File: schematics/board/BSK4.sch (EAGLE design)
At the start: 32 parts

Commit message: Платы подготовлены для Резонита
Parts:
- renumbered U$10 to FS8205A#2, U$5 to DS18B20Z, U$8 to L293DD, U$9 to FS8205A#1
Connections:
- removed net HEAT: DS18B20Z.HEAT, FS8205A#1.HEAT, FS8205A#2.HEAT, L293DD.HEAT
- net GND: now also DS18B20Z.HEAT, FS8205A#1.HEAT, FS8205A#2.HEAT, L293DD.HEAT

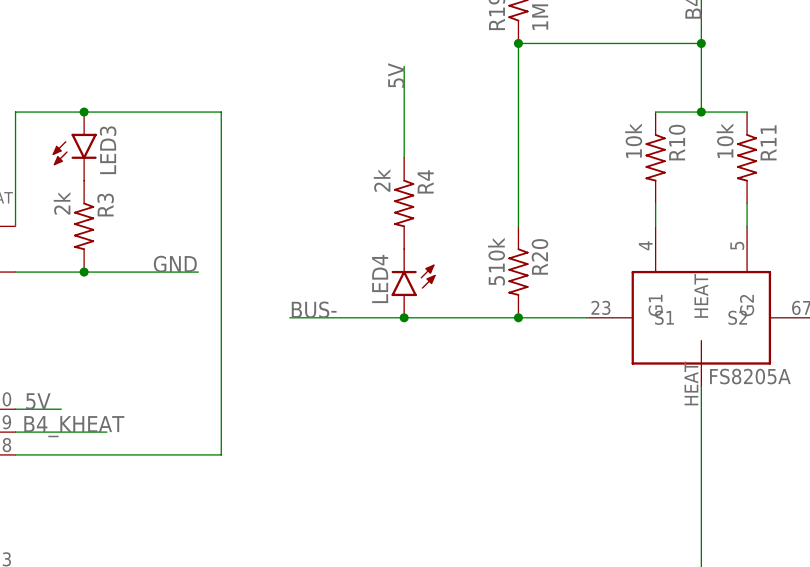
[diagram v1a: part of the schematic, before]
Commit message: Исправлены RADIO и диоды
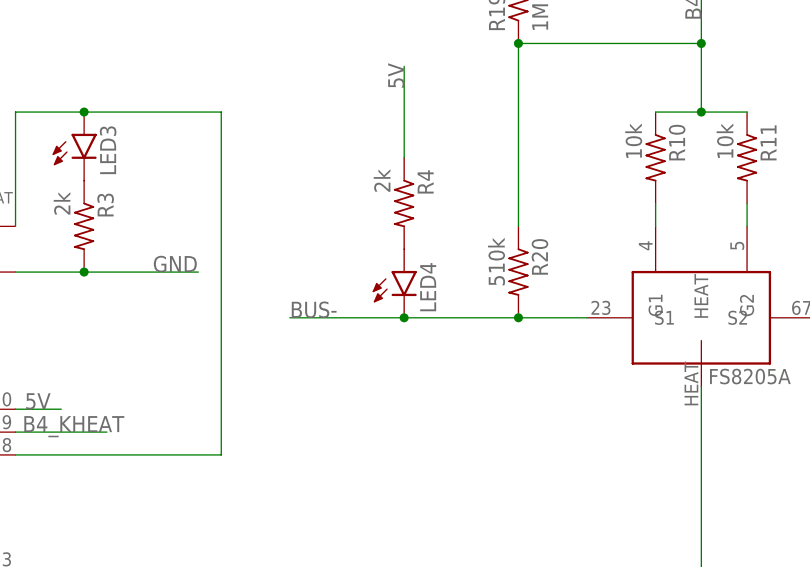
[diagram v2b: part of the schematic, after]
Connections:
- net BUS-: now also LED4.C; no longer LED4.A
- net N$27: now also LED4.A; no longer LED4.C
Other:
- moved on the sheet: LED4
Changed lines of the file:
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@@
 <part name="R3" library="resistor" library_urn="urn:adsk.eagle:library:348" deviceset="R-US_" device="R0603" package3d_urn="urn:adsk.eagle:package:23555/3" value="2k"/>
 <part name="LED3" library="led" library_urn="urn:adsk.eagle:library:259" deviceset="LED" device="CHIPLED_0603" package3d_urn="urn:adsk.eagle:package:15822/2"/>
-<part name="LED4" library="led" library_urn="urn:adsk.eagle:library:259" deviceset="LED" device="CHIPLED_0603" package3d_urn="urn:adsk.eagle:package:15822/2"/>
 <part name="R4" library="resistor" library_urn="urn:adsk.eagle:library:348" deviceset="R-US_" device="R0603" package3d_urn="urn:adsk.eagle:package:23555/3" value="2k"/>
 <part name="LED5" library="led" library_urn="urn:adsk.eagle:library:259" deviceset="LED" device="CHIPLED_0603" package3d_urn="urn:adsk.eagle:package:15822/2"/>
 <part name="R5" library="resistor" library_urn="urn:adsk.eagle:library:348" deviceset="R-US_" device="R0603" package3d_urn="urn:adsk.eagle:package:23555/3" value="2k"/>
+<part name="LED4" library="led" library_urn="urn:adsk.eagle:library:259" deviceset="LED" device="CHIPLED_0603" package3d_urn="urn:adsk.eagle:package:15822/2"/>
 </parts>
 <sheets>
@@
 <attribute name="VALUE" x="92.075" y="234.188" size="1.778" layer="96" rot="R90"/>
 </instance>
-<instance part="LED4" gate="G$1" x="121.92" y="220.98" smashed="yes" rot="R180">
-<attribute name="NAME" x="118.364" y="225.552" size="1.778" layer="95" rot="R270"/>
-<attribute name="VALUE" x="116.205" y="225.552" size="1.778" layer="96" rot="R270"/>
-</instance>
 <instance part="R4" gate="G$1" x="121.92" y="231.14" smashed="yes" rot="R270">
 <attribute name="NAME" x="123.4186" y="234.95" size="1.778" layer="95" rot="R270"/>
@@
 <attribute name="NAME" x="161.5186" y="173.99" size="1.778" layer="95" rot="R270"/>
 <attribute name="VALUE" x="156.718" y="173.99" size="1.778" layer="96" rot="R270"/>
+</instance>
+<instance part="LED4" gate="G$1" x="121.92" y="223.52" smashed="yes">
+<attribute name="NAME" x="125.476" y="218.948" size="1.778" layer="95" rot="R90"/>
+<attribute name="VALUE" x="127.635" y="218.948" size="1.778" layer="96" rot="R90"/>
 </instance>
 </instances>
@@
 <wire x1="134.62" y1="218.44" x2="142.24" y2="218.44" width="0.1524" layer="91"/>
 <pinref part="R20" gate="G$1" pin="2"/>
-<wire x1="134.62" y1="218.44" x2="121.92" y2="218.44" width="0.1524" layer="91"/>
 <junction x="134.62" y="218.44"/>
 <label x="109.22" y="218.44" size="1.778" layer="95"/>
 <pinref part="FS8205A#1" gate="G$1" pin="S1"/>
-<pinref part="LED4" gate="G$1" pin="A"/>
+<wire x1="134.62" y1="218.44" x2="121.92" y2="218.44" width="0.1524" layer="91"/>
+<pinref part="LED4" gate="G$1" pin="C"/>
 <wire x1="121.92" y1="218.44" x2="109.22" y2="218.44" width="0.1524" layer="91"/>
 <junction x="121.92" y="218.44"/>
@@
 </segment>
 </net>
-<net name="N$27" class="0">
-<segment>
-<pinref part="R4" gate="G$1" pin="2"/>
-<pinref part="LED4" gate="G$1" pin="C"/>
-</segment>
-</net>
 <net name="N$28" class="0">
 <segment>
@@
 </segment>
 </net>
+<net name="N$27" class="0">
+<segment>
+<pinref part="LED4" gate="G$1" pin="A"/>
+<pinref part="R4" gate="G$1" pin="2"/>
+</segment>
+</net>

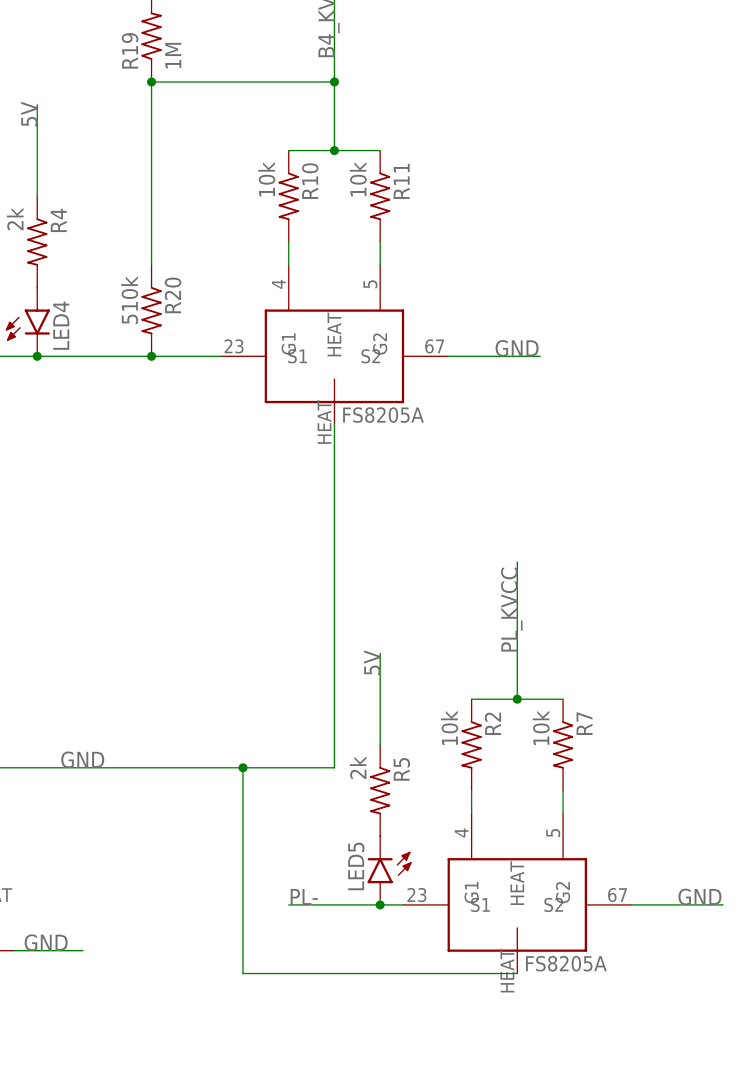
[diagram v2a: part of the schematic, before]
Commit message: Резисторы у FS8205A 100Ом
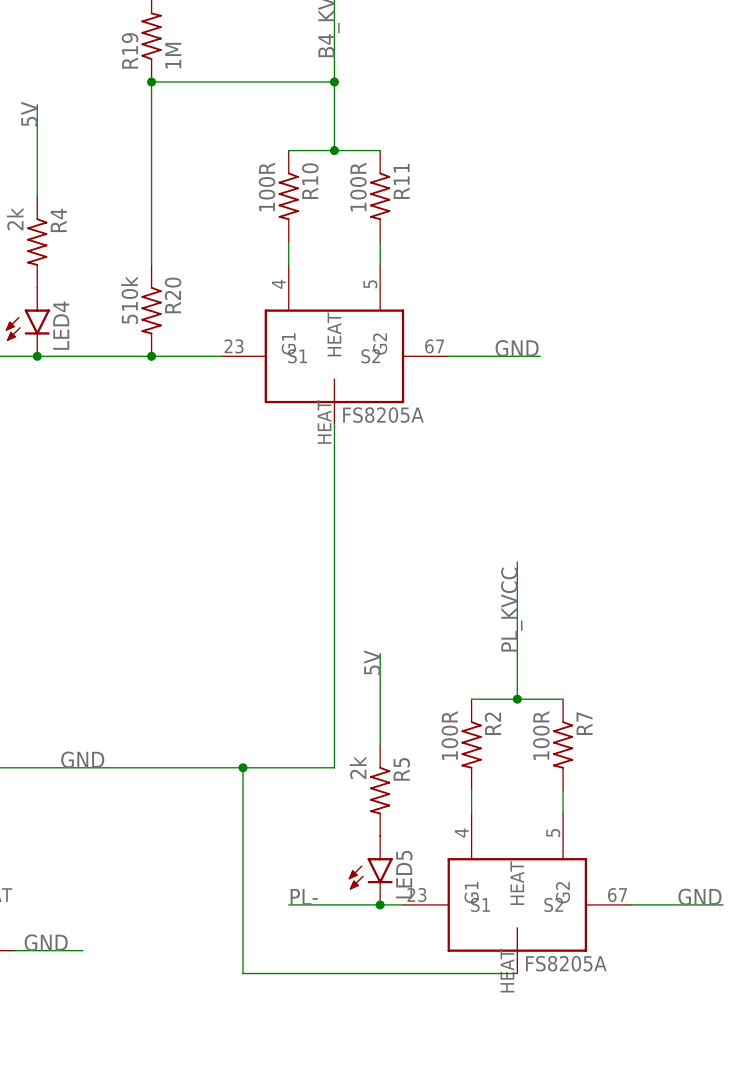
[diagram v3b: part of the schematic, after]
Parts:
- R10, R11, R2, R7: value 10k -> 100R
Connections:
- net N$28: now also LED5.A; no longer LED5.C
- net PL-: now also LED5.C; no longer LED5.A
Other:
- moved on the sheet: LED5
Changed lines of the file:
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@@
 <part name="U$7" library="CanCubeSat" deviceset="EM_HEAT" device=""/>
 <part name="L293DD" library="CanCubeSat" deviceset="L293DD" device=""/>
-<part name="R10" library="resistor" library_urn="urn:adsk.eagle:library:348" deviceset="R-US_" device="R0603" package3d_urn="urn:adsk.eagle:package:23555/3" value="10k"/>
-<part name="R11" library="resistor" library_urn="urn:adsk.eagle:library:348" deviceset="R-US_" device="R0603" package3d_urn="urn:adsk.eagle:package:23555/3" value="10k"/>
+<part name="R10" library="resistor" library_urn="urn:adsk.eagle:library:348" deviceset="R-US_" device="R0603" package3d_urn="urn:adsk.eagle:package:23555/3" value="100R"/>
+<part name="R11" library="resistor" library_urn="urn:adsk.eagle:library:348" deviceset="R-US_" device="R0603" package3d_urn="urn:adsk.eagle:package:23555/3" value="100R"/>
 <part name="R19" library="resistor" library_urn="urn:adsk.eagle:library:348" deviceset="R-US_" device="R0603" package3d_urn="urn:adsk.eagle:package:23555/3" value="1M"/>
 <part name="R20" library="resistor" library_urn="urn:adsk.eagle:library:348" deviceset="R-US_" device="R0603" package3d_urn="urn:adsk.eagle:package:23555/3" value="510k"/>
@@
 <part name="U$21" library="CanCubeSat" deviceset="KCONNECT" device=""/>
 <part name="FS8205A#1" library="CanCubeSat" deviceset="FS8205A+" device=""/>
-<part name="R2" library="resistor" library_urn="urn:adsk.eagle:library:348" deviceset="R-US_" device="R0603" package3d_urn="urn:adsk.eagle:package:23555/3" value="10k"/>
-<part name="R7" library="resistor" library_urn="urn:adsk.eagle:library:348" deviceset="R-US_" device="R0603" package3d_urn="urn:adsk.eagle:package:23555/3" value="10k"/>
+<part name="R2" library="resistor" library_urn="urn:adsk.eagle:library:348" deviceset="R-US_" device="R0603" package3d_urn="urn:adsk.eagle:package:23555/3" value="100R"/>
+<part name="R7" library="resistor" library_urn="urn:adsk.eagle:library:348" deviceset="R-US_" device="R0603" package3d_urn="urn:adsk.eagle:package:23555/3" value="100R"/>
 <part name="BSK1" library="pinheadCS" deviceset="PINHD-1X14" device=""/>
 <part name="PAYLOAD" library="pinheadCS" deviceset="PINHD-1X8" device=""/>
@@
 <part name="LED3" library="led" library_urn="urn:adsk.eagle:library:259" deviceset="LED" device="CHIPLED_0603" package3d_urn="urn:adsk.eagle:package:15822/2"/>
 <part name="R4" library="resistor" library_urn="urn:adsk.eagle:library:348" deviceset="R-US_" device="R0603" package3d_urn="urn:adsk.eagle:package:23555/3" value="2k"/>
-<part name="LED5" library="led" library_urn="urn:adsk.eagle:library:259" deviceset="LED" device="CHIPLED_0603" package3d_urn="urn:adsk.eagle:package:15822/2"/>
 <part name="R5" library="resistor" library_urn="urn:adsk.eagle:library:348" deviceset="R-US_" device="R0603" package3d_urn="urn:adsk.eagle:package:23555/3" value="2k"/>
 <part name="LED4" library="led" library_urn="urn:adsk.eagle:library:259" deviceset="LED" device="CHIPLED_0603" package3d_urn="urn:adsk.eagle:package:15822/2"/>
+<part name="LED5" library="led" library_urn="urn:adsk.eagle:library:259" deviceset="LED" device="CHIPLED_0603" package3d_urn="urn:adsk.eagle:package:15822/2"/>
 </parts>
 <sheets>
@@
 <attribute name="VALUE" x="118.618" y="234.95" size="1.778" layer="96" rot="R270"/>
 </instance>
-<instance part="LED5" gate="G$1" x="160.02" y="160.02" smashed="yes" rot="R180">
-<attribute name="NAME" x="156.464" y="164.592" size="1.778" layer="95" rot="R270"/>
-<attribute name="VALUE" x="154.305" y="164.592" size="1.778" layer="96" rot="R270"/>
-</instance>
 <instance part="R5" gate="G$1" x="160.02" y="170.18" smashed="yes" rot="R270">
 <attribute name="NAME" x="161.5186" y="173.99" size="1.778" layer="95" rot="R270"/>
@@
 <attribute name="NAME" x="125.476" y="218.948" size="1.778" layer="95" rot="R90"/>
 <attribute name="VALUE" x="127.635" y="218.948" size="1.778" layer="96" rot="R90"/>
+</instance>
+<instance part="LED5" gate="G$1" x="160.02" y="162.56" smashed="yes">
+<attribute name="NAME" x="163.576" y="157.988" size="1.778" layer="95" rot="R90"/>
+<attribute name="VALUE" x="165.735" y="157.988" size="1.778" layer="96" rot="R90"/>
 </instance>
 </instances>
@@
 </segment>
 <segment>
-<wire x1="162.56" y1="157.48" x2="160.02" y2="157.48" width="0.1524" layer="91"/>
 <label x="149.86" y="157.48" size="1.778" layer="95"/>
 <pinref part="FS8205A#2" gate="G$1" pin="S1"/>
-<pinref part="LED5" gate="G$1" pin="A"/>
+<wire x1="162.56" y1="157.48" x2="160.02" y2="157.48" width="0.1524" layer="91"/>
+<pinref part="LED5" gate="G$1" pin="C"/>
 <wire x1="160.02" y1="157.48" x2="149.86" y2="157.48" width="0.1524" layer="91"/>
 <junction x="160.02" y="157.48"/>
@@
 </segment>
 </net>
-<net name="N$28" class="0">
-<segment>
-<pinref part="R5" gate="G$1" pin="2"/>
-<pinref part="LED5" gate="G$1" pin="C"/>
-</segment>
-</net>
 <net name="N$27" class="0">
 <segment>
@@
 </segment>
 </net>
+<net name="N$28" class="0">
+<segment>
+<pinref part="LED5" gate="G$1" pin="A"/>
+<pinref part="R5" gate="G$1" pin="2"/>
+</segment>
+</net>

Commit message: Добавлены новые диоды
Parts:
- added LAP4: LAP4-BOTTOM, led:LAP4-BOTTOM
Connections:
- net BUS-: now also LAP4.C
- net N$27: now also LAP4.A
